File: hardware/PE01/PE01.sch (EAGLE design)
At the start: 22 parts, among them IC1 MSP430G2231, IC2 LP2982M5

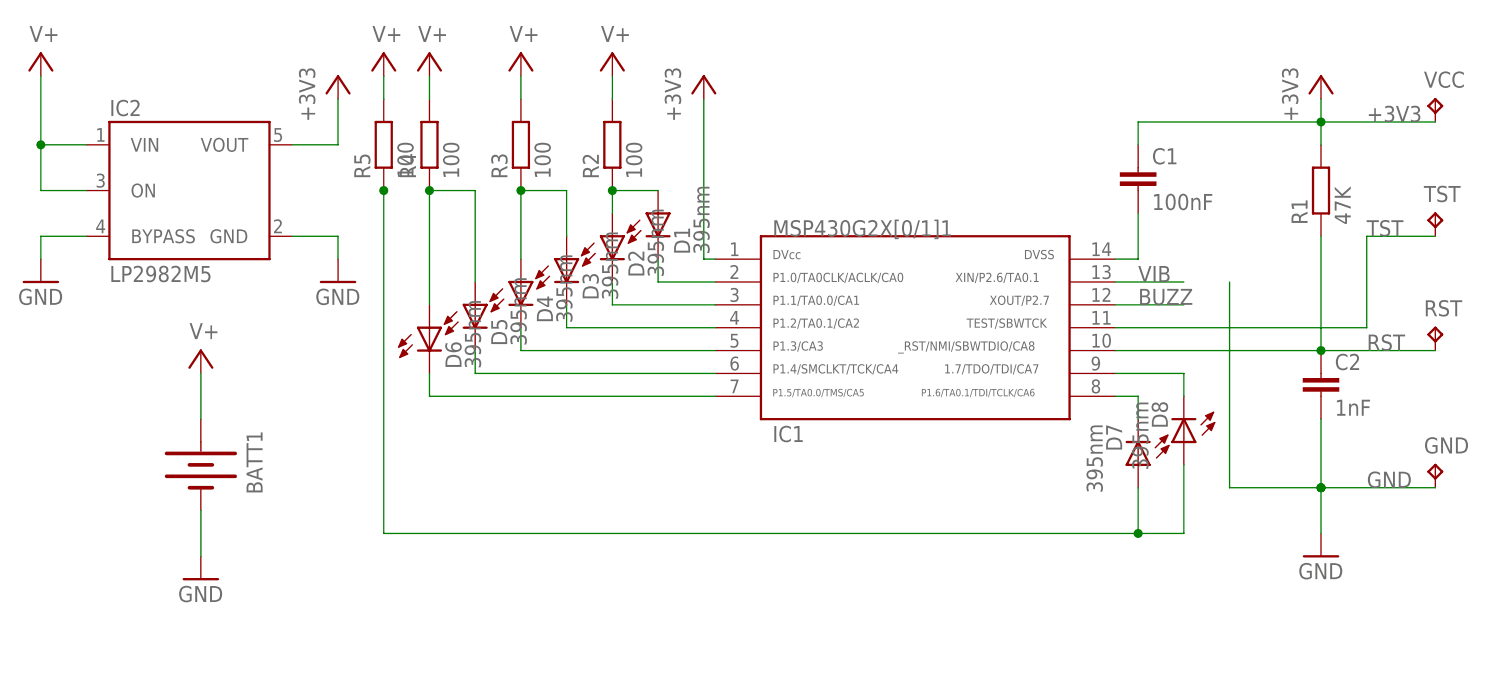
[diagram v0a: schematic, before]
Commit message: Fixed GND, removed slot
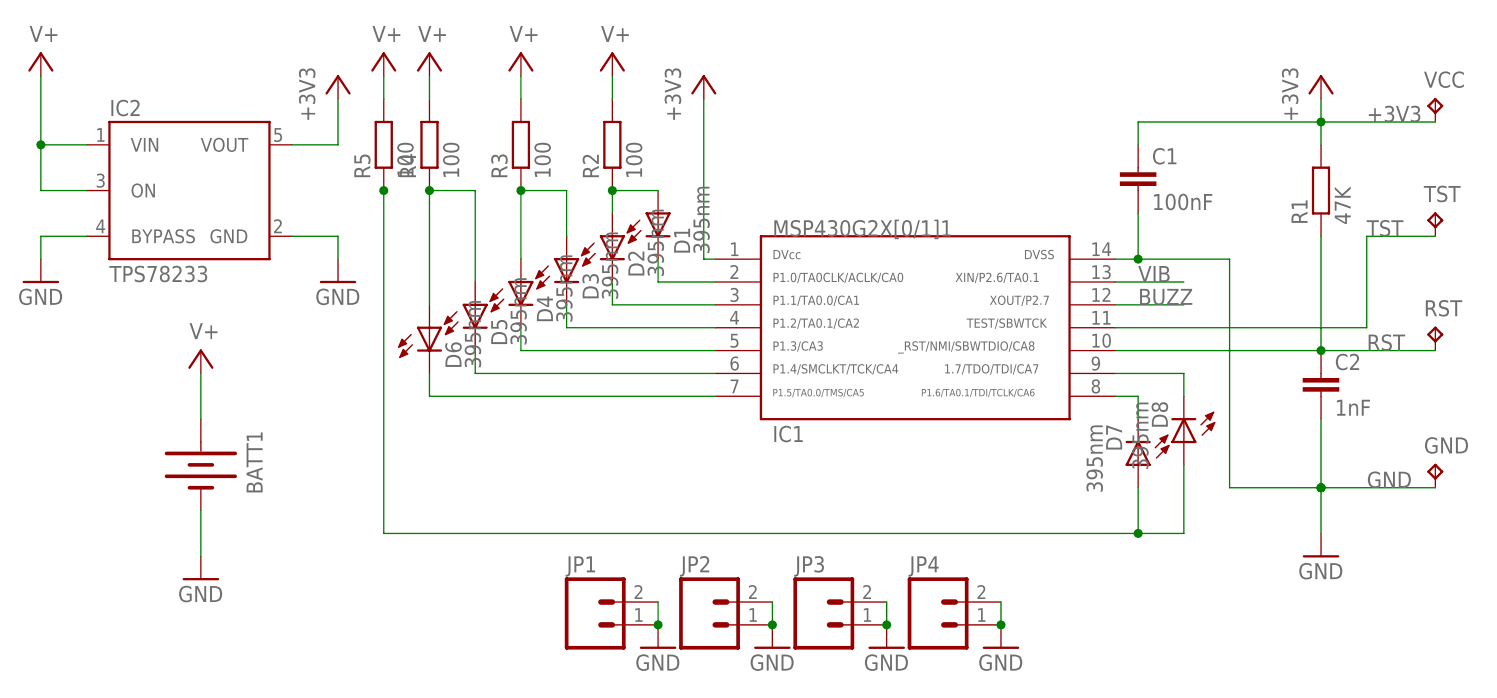
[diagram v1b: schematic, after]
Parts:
- added JP1, JP2, JP3, JP4: (no value), SparkFun:M021X02_NO_SILK
- IC2: value LP2982M5 -> TPS78233
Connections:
- removed net N$13: C1.2, IC1.14
- net GND: now also C1.2, IC1.14, JP1.1, JP1.2, JP2.1, JP2.2, JP3.1, JP3.2, JP4.1, JP4.2
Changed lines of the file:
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@@
 <part name="+3V2" library="supply1" deviceset="+3V3" device=""/>
 <part name="GND3" library="supply1" deviceset="GND" device=""/>
-<part name="IC2" library="v-reg-3" deviceset="LP2982" device="M5"/>
+<part name="IC2" library="v-reg-3" deviceset="LP2982" device="M5" value="TPS78233"/>
 <part name="SUPPLY1" library="supply2" deviceset="V+" device=""/>
 <part name="SUPPLY2" library="supply2" deviceset="V+" device=""/>
@@
 <part name="RST" library="testpad" deviceset="TP" device="TP10R" value="TPTP10R"/>
 <part name="GND" library="testpad" deviceset="TP" device="TP10R" value="TPTP10R"/>
+<part name="JP4" library="SparkFun" deviceset="M02" device="1X02_NO_SILK"/>
+<part name="JP1" library="SparkFun" deviceset="M02" device="1X02_NO_SILK"/>
+<part name="JP2" library="SparkFun" deviceset="M02" device="1X02_NO_SILK"/>
+<part name="JP3" library="SparkFun" deviceset="M02" device="1X02_NO_SILK"/>
+<part name="GND5" library="supply1" deviceset="GND" device=""/>
+<part name="GND6" library="supply1" deviceset="GND" device=""/>
+<part name="GND7" library="supply1" deviceset="GND" device=""/>
+<part name="GND8" library="supply1" deviceset="GND" device=""/>
 </parts>
 <sheets>
@@
 <instance part="RST" gate="G$1" x="104.14" y="58.42"/>
 <instance part="GND" gate="G$1" x="104.14" y="43.18"/>
+<instance part="JP4" gate="G$1" x="48.26" y="25.4"/>
+<instance part="JP1" gate="G$1" x="10.16" y="25.4"/>
+<instance part="JP2" gate="G$1" x="22.86" y="25.4"/>
+<instance part="JP3" gate="G$1" x="35.56" y="25.4"/>
+<instance part="GND5" gate="1" x="17.78" y="22.86"/>
+<instance part="GND6" gate="1" x="30.48" y="22.86"/>
+<instance part="GND7" gate="1" x="43.18" y="22.86"/>
+<instance part="GND8" gate="1" x="55.88" y="22.86"/>
 </instances>
 <busses>
@@
 <pinref part="GND2" gate="1" pin="GND"/>
 <wire x1="91.44" y1="35.56" x2="91.44" y2="40.64" width="0.1524" layer="91"/>
-<wire x1="81.28" y1="40.64" x2="81.28" y2="63.5" width="0.1524" layer="91"/>
+<wire x1="81.28" y1="40.64" x2="81.28" y2="66.04" width="0.1524" layer="91"/>
 <wire x1="81.28" y1="40.64" x2="91.44" y2="40.64" width="0.1524" layer="91"/>
 <wire x1="104.14" y1="40.64" x2="91.44" y2="40.64" width="0.1524" layer="91"/>
 <pinref part="GND" gate="G$1" pin="TP"/>
 <label x="96.52" y="40.64" size="1.778" layer="95"/>
+<pinref part="IC1" gate="G$1" pin="14"/>
+<pinref part="C1" gate="G$1" pin="2"/>
+<wire x1="71.12" y1="71.12" x2="71.12" y2="66.04" width="0.1524" layer="91"/>
+<wire x1="71.12" y1="66.04" x2="68.58" y2="66.04" width="0.1524" layer="91"/>
+<wire x1="71.12" y1="66.04" x2="81.28" y2="66.04" width="0.1524" layer="91"/>
+<junction x="71.12" y="66.04"/>
 </segment>
 <segment>
@@
 <pinref part="GND4" gate="1" pin="GND"/>
 <wire x1="-50.8" y1="68.58" x2="-50.8" y2="66.04" width="0.1524" layer="91"/>
+</segment>
+<segment>
+<pinref part="JP1" gate="G$1" pin="1"/>
+<pinref part="JP1" gate="G$1" pin="2"/>
+<wire x1="17.78" y1="27.94" x2="17.78" y2="25.4" width="0.1524" layer="91"/>
+<junction x="17.78" y="25.4"/>
+<pinref part="GND5" gate="1" pin="GND"/>
+</segment>
+<segment>
+<pinref part="JP2" gate="G$1" pin="1"/>
+<pinref part="JP2" gate="G$1" pin="2"/>
+<wire x1="30.48" y1="27.94" x2="30.48" y2="25.4" width="0.1524" layer="91"/>
+<junction x="30.48" y="25.4"/>
+<pinref part="GND6" gate="1" pin="GND"/>
+</segment>
+<segment>
+<pinref part="JP3" gate="G$1" pin="1"/>
+<pinref part="JP3" gate="G$1" pin="2"/>
+<wire x1="43.18" y1="25.4" x2="43.18" y2="27.94" width="0.1524" layer="91"/>
+<junction x="43.18" y="25.4"/>
+<pinref part="GND7" gate="1" pin="GND"/>
+</segment>
+<segment>
+<pinref part="JP4" gate="G$1" pin="1"/>
+<junction x="55.88" y="25.4"/>
+<pinref part="GND8" gate="1" pin="GND"/>
+<pinref part="JP4" gate="G$1" pin="2"/>
+<wire x1="55.88" y1="25.4" x2="55.88" y2="27.94" width="0.1524" layer="91"/>
 </segment>
 </net>
@@
 </segment>
 </net>
-<net name="N$13" class="0">
-<segment>
-<pinref part="IC1" gate="G$1" pin="14"/>
-<pinref part="C1" gate="G$1" pin="2"/>
-<wire x1="71.12" y1="71.12" x2="71.12" y2="66.04" width="0.1524" layer="91"/>
-<wire x1="71.12" y1="66.04" x2="68.58" y2="66.04" width="0.1524" layer="91"/>
-</segment>
-</net>
